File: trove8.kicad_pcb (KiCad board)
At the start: 4 copper layers, 97 x 115 mm, 101 parts, among them J1 CONN_INPUTS, J2 CONN_OUTPUTS, J3 USB_C, J4 Micro_SD_Card, M1 Module-mcu-0.7, M2 Module-power12-0.2, M3 Module-vr-0.1, M4 Module-knock-0.1, M5 Module-power5-0.2, M6 Module-input-0.1, Q1 ISL9V3040D3ST, Q2 ISL9V3040D3ST, Q3 ISL9V3040D3ST, Q4 ISL9V3040D3ST, Q5 ISL9V3040D3ST, Q6 ISL9V3040D3ST, Q7 ISL9V3040D3ST, Q8 ISL9V3040D3ST, U1 LIS2DW12TR, U10 VNLD5160TR-E, U11 VNLD5160TR-E, U14 VNLD5160TR-E, U3 LPS22HB, U4 TJA1051T-3, U5 SN74LVC4245APWR, U6 VNLD5160TR-E, U7 VNLD5160TR-E, U8 VNLD5160TR-E, U9 VNLD5160TR-E

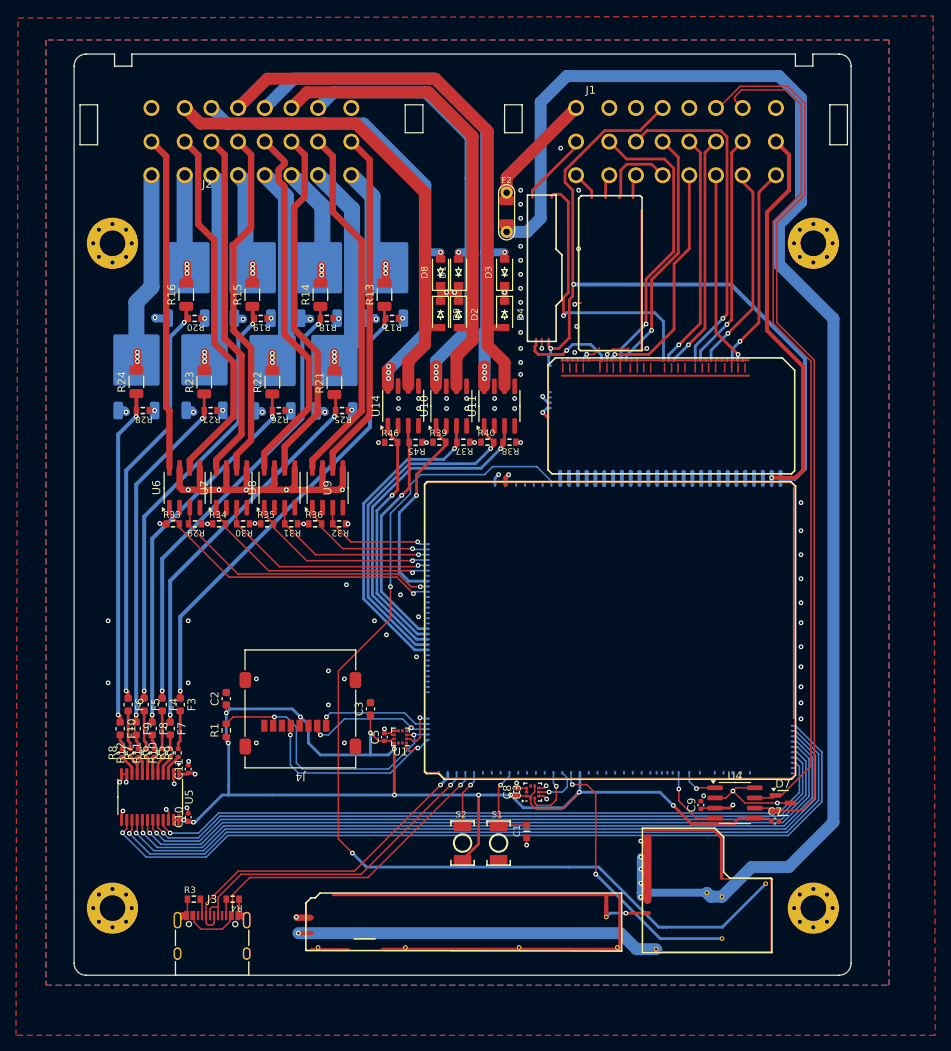
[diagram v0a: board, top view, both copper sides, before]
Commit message: Standalone version without hellen-one
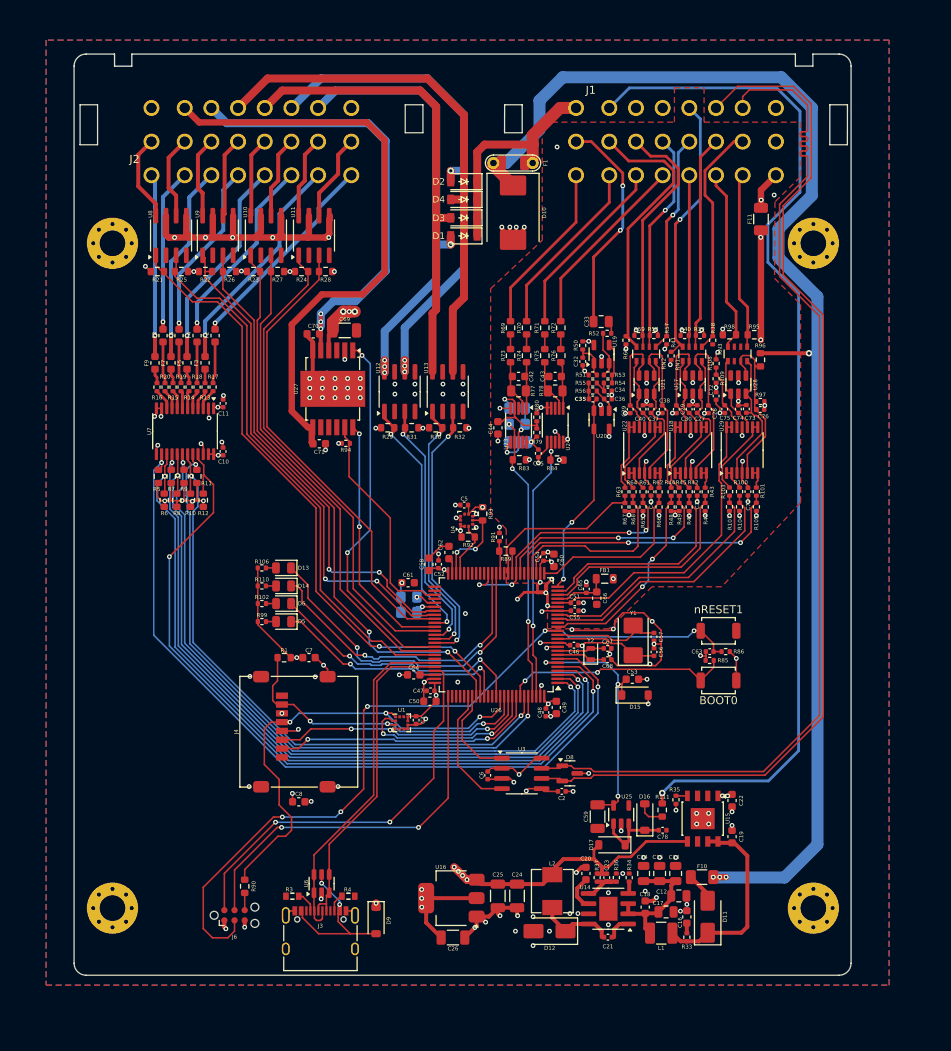
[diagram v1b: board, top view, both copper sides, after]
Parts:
- removed C1: 100n, hellen-one-common:C0603
- removed the D8 at (115.2, 56.8)
- removed M1: Module-mcu-0.7, hellen-one-mcu-0.7:mcu
- removed M2: Module-power12-0.2, hellen-one-power12-0.2:power12
- removed M3: Module-vr-0.1, hellen-one-vr-0.1:vr
- removed M4: Module-knock-0.1, hellen-one-knock-0.1:knock
- removed M5: Module-power5-0.2, hellen-one-power5-0.2:power5
- removed M6: Module-input-0.1, hellen-one-input-0.1:input
- removed Q1, Q2, Q3, Q4, Q5, Q6, Q7, Q8: ISL9V3040D3ST, Package_TO_SOT_SMD:TO-252-2
- removed the R13 at (108.2, 59.5)
- removed the R14 at (100.2, 59.5)
- removed the R15 at (91.8, 59.5)
- removed the R16 at (83.5, 59.5)
- removed the R17 at (109.2, 62.5)
- removed the R18 at (101.0, 62.5)
- removed the R19 at (92.8, 62.5)
- removed the R20 at (84.5, 62.5)
- removed the R21 at (102.0, 70.5)
- removed the R22 at (94.2, 70.5)
- removed the R23 at (85.8, 70.5)
- removed the R24 at (77.3, 70.4)
- removed the R25 at (103.0, 74.0)
- removed the R26 at (95.0, 74.0)
- removed the R27 at (86.5, 74.0)
- removed the R28 at (78.1, 74.0)
- removed S1, S2: Button_SPST, hellen-one-common:SMD-2_2.9x3.9x1.7
- added BOOT0: SW_Push, Button_Switch_SMD:SW_SPST_TS-1088-xR020, F.Cu at (149.9, 107.7)
- added C12: 10u, Capacitor_SMD:C_0805_2012Metric, F.Cu at (145.0, 134.6)
- added C13: 10u, Capacitor_SMD:C_0805_2012Metric, F.Cu at (144.6, 131.8)
- added C14: 10u, Capacitor_SMD:C_0805_2012Metric, F.Cu at (140.6, 131.8)
- added C15: 10u, Capacitor_SMD:C_0805_2012Metric, F.Cu at (142.6, 131.8)
- added C16: 4.7u, Capacitor_SMD:C_0603_1608Metric, F.Cu at (146.0, 137.2)
- added C17: 10u, Capacitor_SMD:C_0805_2012Metric, F.Cu at (143.4, 136.6)
- added C18: 1u, Capacitor_SMD:C_0603_1608Metric, F.Cu at (140.8, 136.0)
- added C19: 1u, Capacitor_SMD:C_0603_1608Metric, F.Cu at (151.6, 127.2)
- added C20: 10n, Capacitor_SMD:C_0603_1608Metric, F.Cu at (133.4, 131.8)
- added C21: 100n, Capacitor_SMD:C_0402_1005Metric, F.Cu at (136.1, 139.8)
- added C22: 1u, Capacitor_SMD:C_0603_1608Metric, F.Cu at (151.6, 122.7)
- added C23: 330p, Capacitor_SMD:C_0402_1005Metric, F.Cu at (136.0, 132.3)
- added C24: 10u, Capacitor_SMD:C_1206_3216Metric, F.Cu at (124.8, 134.6)
- added C25: 47u, Capacitor_SMD:C_1206_3216Metric, F.Cu at (122.4, 134.6)
- added C26: 47u, Capacitor_SMD:C_1206_3216Metric, F.Cu at (116.8, 139.8)
- added C27: 100n, Capacitor_SMD:C_0402_1005Metric, F.Cu at (147.3, 73.8)
- added C28: 100n, Capacitor_SMD:C_0402_1005Metric, F.Cu at (148.7, 73.8)
- added C29: 100n, Capacitor_SMD:C_0402_1005Metric, F.Cu at (144.7, 73.8)
- added C30: 100n, Capacitor_SMD:C_0402_1005Metric, F.Cu at (146.3, 73.8)
- added C31: 100n, Capacitor_SMD:C_0402_1005Metric, F.Cu at (147.3, 84.1)
- added C32: 10n, Capacitor_SMD:C_0402_1005Metric, F.Cu at (133.0, 67.9)
- added C33: 3.3n, Capacitor_SMD:C_0805_2012Metric, F.Cu at (135.3, 62.9)
- added C34: 680p, Capacitor_SMD:C_0402_1005Metric, F.Cu at (136.2, 71.6)
- added C35: 330p, Capacitor_SMD:C_0402_1005Metric, F.Cu at (134.2, 72.6)
- added C36: 47p, Capacitor_SMD:C_0402_1005Metric, F.Cu at (136.2, 72.6)
- added C37: 100n, Capacitor_SMD:C_0402_1005Metric, F.Cu at (141.5, 73.8)
- added C38: 100n, Capacitor_SMD:C_0402_1005Metric, F.Cu at (142.9, 73.8)
- added C39: 100n, Capacitor_SMD:C_0402_1005Metric, F.Cu at (138.9, 73.8)
- added C40: 100n, Capacitor_SMD:C_0402_1005Metric, F.Cu at (140.5, 73.8)
- added C41: 100n, Capacitor_SMD:C_0402_1005Metric, F.Cu at (141.5, 84.1)
- added C42: 1n, Capacitor_SMD:C_0603_1608Metric, F.Cu at (125.0, 69.8)
- added C43: 1n, Capacitor_SMD:C_0603_1608Metric, F.Cu at (129.6, 69.8)
- added C44: 1u, Capacitor_SMD:C_0603_1608Metric, F.Cu at (122.4, 76.2)
- added C45: 100n, Capacitor_SMD:C_0402_1005Metric, F.Cu at (127.5, 79.3)
- added C46: 100n, Capacitor_SMD:C_0402_1005Metric, F.Cu at (131.9, 103.3)
- added C47: 100n, Capacitor_SMD:C_0402_1005Metric, F.Cu at (114.0, 109.0)
- added C48: 100n, Capacitor_SMD:C_0402_1005Metric, F.Cu at (128.4, 111.7)
- added C49: 4.7u, Capacitor_SMD:C_0603_1608Metric, F.Cu at (129.7, 111.1)
- added C50: 4.7u, Capacitor_SMD:C_0603_1608Metric, F.Cu at (113.9, 110.3)
- added C51: 100n, Capacitor_SMD:C_0402_1005Metric, F.Cu at (132.0, 98.0)
- added C52: 100n, Capacitor_SMD:C_0402_1005Metric, F.Cu at (115.0, 93.2)
- added C53: 4.7u, Capacitor_SMD:C_0603_1608Metric, F.Cu at (139.2, 107.5)
- added C54: 100n, Capacitor_SMD:C_0402_1005Metric, F.Cu at (128.1, 92.3)
- added C55: 100n, Capacitor_SMD:C_0402_1005Metric, F.Cu at (132.0, 99.0)
- added C56: 18p, Capacitor_SMD:C_0402_1005Metric, F.Cu at (141.9, 104.2)
- added C57: 18p, Capacitor_SMD:C_0402_1005Metric, F.Cu at (141.9, 102.2)
- added C58: 4.7u, Capacitor_SMD:C_0603_1608Metric, F.Cu at (113.8, 93.2)
- added C59: 47u, Capacitor_SMD:C_1206_3216Metric, F.Cu at (134.8, 124.7)
- added C60: 4.7u, Capacitor_SMD:C_0603_1608Metric, F.Cu at (129.4, 92.7)
- added C61: 1u, Capacitor_SMD:C_0603_1608Metric, F.Cu at (111.2, 95.5)
- added C62: 2.2u, Capacitor_SMD:C_0603_1608Metric, F.Cu at (116.3, 91.7)
- added C63: 100n, Capacitor_SMD:C_0402_1005Metric, F.Cu at (148.8, 104.1)
- added C64: 2.2u, Capacitor_SMD:C_0603_1608Metric, F.Cu at (111.9, 107.0)
- added C65: 100n, Capacitor_SMD:C_0402_1005Metric, F.Cu at (133.4, 96.3)
- added C66: 4.7u, Capacitor_SMD:C_0603_1608Metric, F.Cu at (134.8, 97.4)
- added C67: 12p, Capacitor_SMD:C_0402_1005Metric, F.Cu at (136.1, 103.7)
- added C68: 12p, Capacitor_SMD:C_0402_1005Metric, F.Cu at (136.1, 105.1)
- added C69: 10u, Capacitor_SMD:C_1206_3216Metric, F.Cu at (103.3, 64.0)
- added C70: 10n, Capacitor_SMD:C_0603_1608Metric, F.Cu at (99.4, 64.4)
- added C71: 10n, Capacitor_SMD:C_0603_1608Metric, F.Cu at (100.1, 78.2)
- added C72: 100n, Capacitor_SMD:C_0402_1005Metric, F.Cu at (149.7, 72.2)
- added C73: 100n, Capacitor_SMD:C_0402_1005Metric, F.Cu at (153.4, 73.8)
- added C74: 100n, Capacitor_SMD:C_0402_1005Metric, F.Cu at (152.4, 73.8)
- added C75: 100n, Capacitor_SMD:C_0402_1005Metric, F.Cu at (150.7, 73.8)
- added C76: 1u, Capacitor_SMD:C_0402_1005Metric, F.Cu at (155.2, 73.9)
- added C77: 100n, Capacitor_SMD:C_0402_1005Metric, F.Cu at (153.6, 84.1)
- added C78: 100n, Capacitor_SMD:C_0402_1005Metric, F.Cu at (143.0, 126.4)
- added D10: SM15T33CA, Diode_SMD:D_SMC, F.Cu at (124.3, 49.3)
- added D11: SS34, Diode_SMD:D_SMA, F.Cu at (148.6, 137.2)
- added D12: SS34, Diode_SMD:D_SMA, F.Cu at (128.8, 139.0)
- added D13: BLUE, LED_SMD:LED_0805_2012Metric, F.Cu at (95.6, 93.7)
- added D14: YELLOW, LED_SMD:LED_0805_2012Metric, F.Cu at (95.7, 95.9)
- added D15: 1N5819WS, Diode_SMD:D_SOD-123, F.Cu at (139.5, 109.5)
- added D16: 1N5819WS, Diode_SMD:D_SOD-123, F.Cu at (140.8, 124.8)
- added D17: 1N5819WS, Diode_SMD:D_SOD-123, F.Cu at (136.7, 128.2)
- added D5: RED, LED_SMD:LED_0805_2012Metric, F.Cu at (95.7, 100.3)
- added D6: GREEN, LED_SMD:LED_0805_2012Metric, F.Cu at (95.7, 98.1)
- added F10: Polyfuse, Fuse:Fuse_1206_3216Metric, F.Cu at (147.9, 132.2)
- added F11: 120mA, Fuse:Fuse_1206_3216Metric, F.Cu at (155.2, 50.1)
- added FB1: Ferrite_Bead, Inductor_SMD:L_0805_2012Metric, F.Cu at (135.8, 95.0)
- added J6: Conn_01x06, Connector:Tag-Connect_TC2030-IDC-NL_2x03_P1.27mm_Vertical, F.Cu at (89.5, 137.0)
- added JP1: Jumper_3_Bridged12, Jumper:SolderJumper-3_P1.3mm_Bridged12_RoundedPad1.0x1.5mm, B.Cu at (125.0, 78.0)
- added L1: 2.2u, Inductor_SMD:L_1210_3225Metric, F.Cu at (142.8, 139.2)
- added L2: 10u, sunlord-MWSA0503:MWSA0503, F.Cu at (129.2, 134.0)
- added NT1: NetTie_2, NetTie:NetTie-2_SMD_Pad0.5mm, F.Cu at (127.8, 96.7)
- added R10: 4.7k, Resistor_SMD:R_0603_1608Metric, F.Cu at (84.0, 85.2)
- added R100: 4k7, Resistor_SMD:R_0402_1005Metric, F.Cu at (152.6, 84.1)
- added R101: 4k7, Resistor_SMD:R_0402_1005Metric, F.Cu at (154.7, 84.1)
- added R102: 470, Resistor_SMD:R_0402_1005Metric, F.Cu at (93.0, 98.1)
- added R103: 4k7, Resistor_SMD:R_0402_1005Metric, F.Cu at (151.3, 84.1)
- added R104: 4k7, Resistor_SMD:R_0402_1005Metric, F.Cu at (152.6, 86.0)
- added R105: 4k7, Resistor_SMD:R_0402_1005Metric, F.Cu at (154.7, 86.0)
- added R106: 470, Resistor_SMD:R_0402_1005Metric, F.Cu at (92.9, 93.7)
- added R107: 4k7, Resistor_SMD:R_0402_1005Metric, F.Cu at (151.3, 86.0)
- added R108: 4k7, Resistor_SMD:R_0402_1005Metric, F.Cu at (149.7, 68.1)
- added R109: 4k7, Resistor_SMD:R_0402_1005Metric, F.Cu at (149.7, 70.0)
- added R11: 4.7k, Resistor_SMD:R_0603_1608Metric, F.Cu at (84.8, 82.2)
- added R110: 470, Resistor_SMD:R_0402_1005Metric, F.Cu at (92.9, 95.9)
- added R111: 6.8k, Resistor_SMD:R_0603_1608Metric, F.Cu at (142.9, 123.9)
- added R12: 4.7k, Resistor_SMD:R_0603_1608Metric, F.Cu at (85.6, 85.2)
- added R33: 1, Resistor_SMD:R_0402_1005Metric, F.Cu at (146.0, 139.8)
- added R34: 10k, Resistor_SMD:R_0402_1005Metric, F.Cu at (138.8, 132.3)
- added R35: 10k, Resistor_SMD:R_0402_1005Metric, F.Cu at (144.6, 122.6)
- added R36: 12k, Resistor_SMD:R_0402_1005Metric, F.Cu at (137.2, 132.3)
- added R37: 68k, Resistor_SMD:R_0402_1005Metric, F.Cu at (134.8, 132.3)
- added R38: 470k, Resistor_SMD:R_0402_1005Metric, F.Cu at (149.2, 65.2)
- added R39: 470k, Resistor_SMD:R_0402_1005Metric, F.Cu at (147.6, 64.6)
- added R40: 470k, Resistor_SMD:R_0402_1005Metric, F.Cu at (145.7, 64.6)
- added R41: 470k, Resistor_SMD:R_0402_1005Metric, F.Cu at (144.0, 67.2)
- added R42: 4k7, Resistor_SMD:R_0402_1005Metric, F.Cu at (146.3, 84.1)
- added R43: 4k7, Resistor_SMD:R_0402_1005Metric, F.Cu at (148.3, 84.1)
- added R44: 4k7, Resistor_SMD:R_0402_1005Metric, F.Cu at (144.0, 84.1)
- added R47: 4k7, Resistor_SMD:R_0402_1005Metric, F.Cu at (148.3, 86.0)
- added R48: 4k7, Resistor_SMD:R_0402_1005Metric, F.Cu at (144.0, 86.0)
- added R49: 4k7, Resistor_SMD:R_0402_1005Metric, F.Cu at (145.0, 86.0)
- added R5: 4.7k, Resistor_SMD:R_0603_1608Metric, F.Cu at (80.0, 82.2)
- added R50: 33k, Resistor_SMD:R_0402_1005Metric, F.Cu at (133.0, 65.9)
- added R51: 33k, Resistor_SMD:R_0402_1005Metric, F.Cu at (134.2, 69.6)
- added R52: 100k, Resistor_SMD:R_0402_1005Metric, F.Cu at (136.1, 64.4)
- added R53: 470k, Resistor_SMD:R_0402_1005Metric, F.Cu at (136.2, 69.6)
- added R54: 12k, Resistor_SMD:R_0402_1005Metric, F.Cu at (136.2, 70.6)
- added R55: 100k, Resistor_SMD:R_0402_1005Metric, F.Cu at (134.2, 70.6)
- added R56: 33k, Resistor_SMD:R_0402_1005Metric, F.Cu at (134.2, 71.6)
- added R57: 470k, Resistor_SMD:R_0402_1005Metric, F.Cu at (143.5, 65.2)
- added R58: 470k, Resistor_SMD:R_0402_1005Metric, F.Cu at (141.9, 64.6)
- added R59: 470k, Resistor_SMD:R_0402_1005Metric, F.Cu at (140.0, 64.6)
- added R6: 4.7k, Resistor_SMD:R_0603_1608Metric, F.Cu at (80.8, 85.2)
- added R60: 470k, Resistor_SMD:R_0402_1005Metric, F.Cu at (138.4, 65.2)
- added R61: 4k7, Resistor_SMD:R_0402_1005Metric, F.Cu at (140.5, 84.1)
- added R62: 4k7, Resistor_SMD:R_0402_1005Metric, F.Cu at (142.5, 84.1)
- added R63: 4k7, Resistor_SMD:R_0402_1005Metric, F.Cu at (138.3, 84.1)
- added R64: 4k7, Resistor_SMD:R_0402_1005Metric, F.Cu at (139.3, 84.1)
- added R65: 4k7, Resistor_SMD:R_0402_1005Metric, F.Cu at (140.5, 86.0)
- added R66: 4k7, Resistor_SMD:R_0402_1005Metric, F.Cu at (142.5, 86.0)
- added R67: 4k7, Resistor_SMD:R_0402_1005Metric, F.Cu at (138.3, 86.0)
- added R68: 4k7, Resistor_SMD:R_0402_1005Metric, F.Cu at (139.3, 86.0)
- added R69: 4.7k, Resistor_SMD:R_0603_1608Metric, F.Cu at (124.0, 63.7)
- added R7: 4.7k, Resistor_SMD:R_0603_1608Metric, F.Cu at (81.6, 82.2)
- added R70: 4.7k, Resistor_SMD:R_0603_1608Metric, F.Cu at (126.0, 63.7)
- added R71: 4.7k, Resistor_SMD:R_0603_1608Metric, F.Cu at (128.3, 63.7)
- added R72: 4.7k, Resistor_SMD:R_0603_1608Metric, F.Cu at (130.3, 63.7)
- added R73: 4.7k, Resistor_SMD:R_0603_1608Metric, F.Cu at (124.0, 67.2)
- added R74: 4.7k, Resistor_SMD:R_0603_1608Metric, F.Cu at (126.0, 67.2)
- added R75: 4.7k, Resistor_SMD:R_0603_1608Metric, F.Cu at (128.3, 67.2)
- added R76: 4.7k, Resistor_SMD:R_0603_1608Metric, F.Cu at (130.3, 67.2)
- added R77: DNP, Resistor_SMD:R_0805_2012Metric, F.Cu at (125.0, 71.5)
- added R78: DNP, Resistor_SMD:R_0805_2012Metric, F.Cu at (129.6, 71.5)
- added R79: 1k, Resistor_SMD:R_0402_1005Metric, F.Cu at (127.3, 76.8)
- added R8: 4.7k, Resistor_SMD:R_0603_1608Metric, F.Cu at (82.3, 85.2)
- added R80: 1k, Resistor_SMD:R_0402_1005Metric, F.Cu at (127.3, 74.8)
- added R81: DNP, Resistor_SMD:R_0805_2012Metric_Pad1.20x1.40mm_HandSolder, B.Cu at (124.8, 73.7)
- added R82: DNP, Resistor_SMD:R_0805_2012Metric_Pad1.20x1.40mm_HandSolder, B.Cu at (124.8, 75.7)
- added R83: 4.7k, Resistor_SMD:R_0603_1608Metric, F.Cu at (125.1, 80.2)
- added R84: 4.7k, Resistor_SMD:R_0603_1608Metric, F.Cu at (129.8, 80.2)
- added R85: 10k, Resistor_SMD:R_0402_1005Metric, F.Cu at (148.8, 105.2)
- added R86: 10k, Resistor_SMD:R_0402_1005Metric, F.Cu at (150.8, 104.1)
- added R87: DNP, Resistor_SMD:R_0805_2012Metric_Pad1.20x1.40mm_HandSolder, B.Cu at (111.3, 97.3)
- added R88: DNP, Resistor_SMD:R_0805_2012Metric_Pad1.20x1.40mm_HandSolder, B.Cu at (111.3, 99.2)
- added R89: 0, Resistor_SMD:R_0603_1608Metric, F.Cu at (123.4, 91.5)
- added R9: 4.7k, Resistor_SMD:R_0603_1608Metric, F.Cu at (83.2, 82.2)
- added R90: 100, Resistor_SMD:R_0603_1608Metric, F.Cu at (90.8, 133.4)
- added R91: 10k, Resistor_SMD:R_0402_1005Metric, F.Cu at (122.6, 89.8)
- added R92: 2k2, Resistor_SMD:R_0603_1608Metric, F.Cu at (118.7, 89.8)
- added R93: 2k2, Resistor_SMD:R_0603_1608Metric, F.Cu at (120.5, 86.9)
- added R94: 10k, Resistor_SMD:R_0402_1005Metric, F.Cu at (103.4, 78.1)
- added R95: 2.7k, Resistor_SMD:R_0603_1608Metric, F.Cu at (154.4, 64.5)
- added R96: 48.7k, Resistor_SMD:R_0603_1608Metric, F.Cu at (155.2, 67.7)
- added R97: 10k, Resistor_SMD:R_0402_1005Metric, F.Cu at (155.2, 72.9)
- added R98: 2.7k, Resistor_SMD:R_0603_1608Metric, F.Cu at (151.3, 64.5)
- added R99: 470, Resistor_SMD:R_0402_1005Metric, F.Cu at (93.0, 100.3)
- added RN1: 10k, Resistor_SMD:R_Array_Convex_4x0603, F.Cu at (146.7, 66.9)
- added RN2: 10k, Resistor_SMD:R_Array_Convex_4x0603, F.Cu at (140.9, 66.9)
- added RN3: 10k, Resistor_SMD:R_Array_Convex_4x0603, F.Cu at (152.3, 66.9)
- added U15: TLS115, Package_SO:Infineon_PG-DSO-8-43, F.Cu at (148.0, 125.0)
- added U16: AMS1117-3.3, Package_TO_SOT_SMD:SOT-223-3_TabPin2, F.Cu at (116.6, 134.9)
- added U17: SRV05-4, Package_TO_SOT_SMD:SOT-23-6, F.Cu at (146.7, 70.8)
- added U18: MCP6004, Package_SO:TSSOP-14_4.4x5mm_P0.65mm, F.Cu at (146.5, 78.9)
- added U19: LMV321, Package_TO_SOT_SMD:SOT-23-5, F.Cu at (135.3, 67.0)
- added U20: LMV321, Package_TO_SOT_SMD:SOT-23-5, F.Cu at (135.3, 75.2)
- added U21: SRV05-4, Package_TO_SOT_SMD:SOT-23-6, F.Cu at (141.0, 70.8)
- added U22: MCP6004, Package_SO:TSSOP-14_4.4x5mm_P0.65mm, F.Cu at (140.7, 78.9)
- added U23: MAX9924, Package_SO:MSOP-10_3x3mm_P0.5mm, F.Cu at (125.0, 75.8)
- added U24: MAX9924, Package_SO:MSOP-10_3x3mm_P0.5mm, F.Cu at (129.6, 75.8)
- added U25: MIC5205-3.3YM5, Package_TO_SOT_SMD:SOT-23-5, F.Cu at (137.8, 124.5)
- added U26: STM32F427VGTx, Package_QFP:LQFP-100_14x14mm_P0.5mm, F.Cu at (122.2, 102.0)
- added U27: TLE9201SG, Package_SO:Infineon_PG-DSO-12-9, F.Cu at (101.8, 71.3)
- added U28: SRV05-4, Package_TO_SOT_SMD:SOT-23-6, F.Cu at (152.4, 70.8)
- added U29: MCP6004, Package_SO:TSSOP-14_4.4x5mm_P0.65mm, F.Cu at (152.9, 78.9)
- added U6: USBLC6-2SC6, Package_TO_SOT_SMD:SOT-23-6, F.Cu at (100.4, 133.1)
- added Y1: 20MHz, Crystal:Crystal_SMD_5032-2Pin_5.0x3.2mm, F.Cu at (139.3, 102.7)
- added Y2: 32.768 kHz, Crystal:Crystal_SMD_2012-2Pin_2.0x1.2mm, F.Cu at (134.0, 104.4)
- added nRESET1: SW_Push, Button_Switch_SMD:SW_SPST_TS-1088-xR020, F.Cu at (149.9, 101.5)
- D9: value B5819W -> 1N5819WS; footprint hellen-one-common:SOD-123 -> Diode_SMD:D_SOD-123
- J2: footprint Connector_Automotive:Delphi_Sicma_24_Black -> Connector_Automotive:Delphi_Sicma_24_Grey
- R21: renamed from R33; footprint hellen-one-common:R0603 -> Resistor_SMD:R_0603_1608Metric
- R22: renamed from R34; footprint hellen-one-common:R0603 -> Resistor_SMD:R_0603_1608Metric
- R23: renamed from R35; footprint hellen-one-common:R0603 -> Resistor_SMD:R_0603_1608Metric
- R24: renamed from R36; footprint hellen-one-common:R0603 -> Resistor_SMD:R_0603_1608Metric
- R25: renamed from R29; footprint hellen-one-common:R0603 -> Resistor_SMD:R_0603_1608Metric
- R26: renamed from R30; footprint hellen-one-common:R0603 -> Resistor_SMD:R_0603_1608Metric
- R27: renamed from R31; footprint hellen-one-common:R0603 -> Resistor_SMD:R_0603_1608Metric
- R28: renamed from R32; footprint hellen-one-common:R0603 -> Resistor_SMD:R_0603_1608Metric
- R29: renamed from R39; footprint hellen-one-common:R0603 -> Resistor_SMD:R_0603_1608Metric
- R30: renamed from R40; footprint hellen-one-common:R0603 -> Resistor_SMD:R_0603_1608Metric
- R31: renamed from R37; footprint hellen-one-common:R0603 -> Resistor_SMD:R_0603_1608Metric
- R32: renamed from R38; footprint hellen-one-common:R0603 -> Resistor_SMD:R_0603_1608Metric
- R45, R46: value 4.7k -> 4k7; footprint hellen-one-common:R0603 -> Resistor_SMD:R_0402_1005Metric
- U14: value VNLD5160TR-E -> LMR14020; footprint Package_SO:SOIC-8_3.9x4.9mm_P1.27mm -> Package_SO:SOIC-8-1EP_3.9x4.9mm_P1.27mm_EP2.29x3mm
- moved D9 76.1 mm to (107.2, 137.7)
- moved U14 67.8 mm to (136.2, 136.2), turned to 180 degrees
- moved F2 46.3 mm to (87.1, 64.7)
- moved F4 46.3 mm to (84.8, 64.7)
- moved F6 46.3 mm to (82.6, 64.7)
- moved F8 46.3 mm to (80.6, 64.7)
- moved F3 45.9 mm to (85.8, 68.0)
- moved F5 45.9 mm to (83.6, 68.0)
- moved F7 45.9 mm to (81.6, 68.0)
- moved F9 45.9 mm to (79.6, 68.0)
- moved C10 45.9 mm to (88.1, 79.1)
- moved C11 45.9 mm to (88.1, 73.1)
- moved R13 45.9 mm to (85.8, 71.1)
- moved R14 45.9 mm to (83.8, 71.1)
- moved R15 45.9 mm to (81.8, 71.1)
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- renumbered C7 to C2, C5 to C3, C8 to C5, C9 to C6, C2 to C7, C3 to C8, D7 to D8, F2 to F1, F3 to F2, F7 to F3, F8 to F5, F5 to F6, F9 to F7, F6 to F8, F10 to F9, R5 to R13, R6 to R14, R7 to R15, R8 to R16, R9 to R17, R10 to R18, R11 to R19, R12 to R20, U8 to U10, U9 to U11, U10 to U12, U11 to U13, U4 to U3, U3 to U4, U5 to U7, U6 to U8, U7 to U9
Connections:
- net /Injection/IN1 renamed /MCU_INJ1
- net /Injection/IN2 renamed /MCU_INJ2
- net /Injection/IN3 renamed /MCU_INJ3
- net /Injection/IN4 renamed /MCU_INJ4
- net /Injection/IN5 renamed /MCU_INJ5
- net /Injection/IN6 renamed /MCU_INJ6
- net /Injection/IN7 renamed /MCU_INJ7
- net /Injection/IN8 renamed /MCU_INJ8
- net /LS6/IN1 renamed /MCU_PWM1
- net /LS6/IN2 renamed /MCU_PWM2
- net /LS6/IN3 renamed /MCU_PWM3
- net /LS6/IN4 renamed /MCU_PWM4
- net /USB+ renamed /USB_D+
- net /USB- renamed /USB_D-
- D1 pad 1: +12V_RAW -> +12V_IN
- D2 pad 1: +12V_RAW -> +12V_IN
- D3 pad 1: +12V_RAW -> +12V_IN
- D4 pad 1: +12V_RAW -> +12V_IN
- D9 pad 1: +12V_RAW -> +5V
- D9 pad 2: /OUT_LS6 -> /USB_VBUS
- F2 pad 1: Net-(F3-Pad1) -> /IGN_8
- F3 pad 1: Net-(F7-Pad1) -> /IGN_7
- F4 pad 1: Net-(F4-Pad1) -> /IGN_6
- F5 pad 1: Net-(F8-Pad1) -> /IGN_5
- F6 pad 1: Net-(F5-Pad1) -> /IGN_4
- F7 pad 1: Net-(F9-Pad1) -> /IGN_3
- F8 pad 1: Net-(F6-Pad1) -> /IGN_2
- F9 pad 1: Net-(F10-Pad1) -> /IGN_1
- H1 pad 1: (no net) -> GND
- H2 pad 1: (no net) -> GND
- H3 pad 1: (no net) -> GND
- H4 pad 1: (no net) -> GND
- J1 pad A1: /IN_CRANK_NEGATIVE -> /IN_CRANK_PRIMARY
- J1 pad A2: /IN_CRANK_PRIMARY -> /IN_CRANK_NEGATIVE
- J1 pad A3: /IN_CAM_NEGATIVE -> /IN_CAM_PRIMARY
- J1 pad A4: /IN_CAM_PRIMARY -> /IN_CAM_NEGATIVE
- J1 pad A5: /IN_O2S -> /IN_MAP
- J1 pad A6: /IN_O2S2 -> /IN_IAT
- J1 pad A7: /IN_PPS2 -> /IN_CLT
- J1 pad A8: /IN_PPS1 -> Net-(F11-Pad2)
- J1 pad B4: /IN_MAP -> /IN_PPS1
- J1 pad B5: /IN_CLT -> /IN_PPS2
- J1 pad B6: /IN_IAT -> /IN_O2S2
- J1 pad B7: /IN_AC_CLUTCH -> /IN_O2S
- J1 pad C2: +12V_KEY -> +12V_PERM
- J1 pad C4: +5VA -> unconnected-(J1-PadC4)
- J1 pad C5: unconnected-(J1-PadC5) -> /IN_AC_CLUTCH
- J2 pad C2: /OUT_LS6 -> /OUT_DL
- J2 pad C3: /OUT_LS5 -> /OUT_DH
- J4 pad 1: /SD_CS -> unconnected-(J4-DAT2-Pad1)
- J4 pad 2: /SPI1_MOSI -> /SD_CS
- J4 pad 3: GND -> /SPI1_MOSI
- R45 pad 1: GND -> /MCU_IN_AC_CLUTCH
- R45 pad 2: /LS6/IN6 -> Net-(U18C--)
- R46 pad 1: GND -> GNDA
- R46 pad 2: /LS6/IN5 -> /MCU_IN_O2S
- U14 pad 1: /LS6/IN5 -> Net-(U14-BOOT)
- U14 pad 2: unconnected-(U14-STATUS1-Pad2) -> /VReg/12V_PRE
- U14 pad 3: /LS6/IN6 -> /VReg/12V_PRE
- U14 pad 4: unconnected-(U14-STATUS2-Pad4) -> Net-(U14-RT)
- U14 pad 5: GND -> Net-(U14-FB)
- U14 pad 6: /OUT_LS6 -> Net-(U14-SS)
- U14 pad 8: /OUT_LS5 -> Net-(D12-K)
- U3 pad 1: /CAN1_RX -> /CAN1_TX
- U3 pad 4: /CAN1_TX -> /CAN1_RX
- U7 pad 14: /Ignition/IN8 -> /MCU_IGN1
- U7 pad 15: /Ignition/IN7 -> /MCU_IGN2
- U7 pad 16: /Ignition/IN6 -> /MCU_IGN3
- U7 pad 17: /Ignition/IN5 -> /MCU_IGN4
- U7 pad 18: /Ignition/IN4 -> /MCU_IGN5
- U7 pad 19: /Ignition/IN3 -> /MCU_IGN6
- U7 pad 20: /Ignition/IN2 -> /MCU_IGN7
- U7 pad 21: /Ignition/IN1 -> /MCU_IGN8
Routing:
- net +3.3V: track 158.8 -> 423.6 mm, vias 12 -> 27
- net GND: track 101.7 -> 244.5 mm, vias 99 -> 124
- net +12V_PERM: track 0.00 -> 129.7 mm, vias 0 -> 1
- net /VIGN: track 127.9 -> 0.00 mm, vias 2 -> 0
- net /Ignition/IN8: track 104.5 -> 0.00 mm, vias 1 -> 0
- net /Ignition/IN7: track 101.9 -> 0.00 mm, vias 1 -> 0
- net /MCU_IGN8: track 0.00 -> 99.9 mm, vias 0 -> 2
- net /MCU_IGN1: track 0.00 -> 99.4 mm, vias 0 -> 2
- net /Ignition/IN6: track 99.4 -> 0.00 mm, vias 1 -> 0
- net /MCU/nRESET: track 0.00 -> 98.8 mm, vias 0 -> 5
- net /Ignition/IN5: track 96.9 -> 0.00 mm, vias 1 -> 0
- net /MCU_IGN2: track 0.00 -> 95.5 mm, vias 0 -> 2
- net /Ignition/IN4: track 94.5 -> 0.00 mm, vias 1 -> 0
- net /Ignition/IN3: track 92.0 -> 0.00 mm, vias 1 -> 0
- net /MCU_IGN3: track 0.00 -> 91.1 mm, vias 0 -> 2
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- added copper zone on F.Cu, net GNDA
- added copper zone on In2.Cu, net GNDA
